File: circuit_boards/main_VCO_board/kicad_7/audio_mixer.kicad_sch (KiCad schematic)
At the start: 24 parts, among them U14 TL072

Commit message: Progress on circuit boards
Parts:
- added D1406 (x5): XLMDK65D, LED_THT:LED_D3.0mm, symbol Device:LED
- added R908, R909, R910, R912: 12k, Resistor_SMD:R_0603_1608Metric, symbol Device:R
- added R911: 5k6, Resistor_SMD:R_0603_1608Metric, symbol Device:R
- SW? (x4): value E-Switch_EG2201 -> E-Switch_EG2201B
- SW? (x5): value E-Switch_EG2301 -> E-Switch_EG2301B
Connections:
- net GND: now also D1406.1 (K), D1406.1 (K), D1406.1 (K), D1406.1 (K), D1406.1 (K)
- net +12V: now reaches SW?.1
- net +12V: now also SW?.1, SW?.1, SW?.1, SW?.2, SW?.2
- net at SW?.3: now also R910.1
- net at SW?.3: now also R912.1
- net at RV10.3, SW?.3: now also R911.1
- net at SW?.2: now also R909.1
- net at SW?.2: now also R908.1
- new net: D1406.2 (A), R908.2
- new net: D1406.2 (A), R909.2
- new net: D1406.2 (A), R910.2
- new net: D1406.2 (A), R911.2
- new net: D1406.2 (A), R912.2
- no-connect marks 14 -> 4
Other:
- note added: "AUDIO SOURCE ENABLED INDICATORS"
- moved on the sheet: C901, R901, R902, R903, R904, R905, R906, R907, RV10, RV11, RV7, RV8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

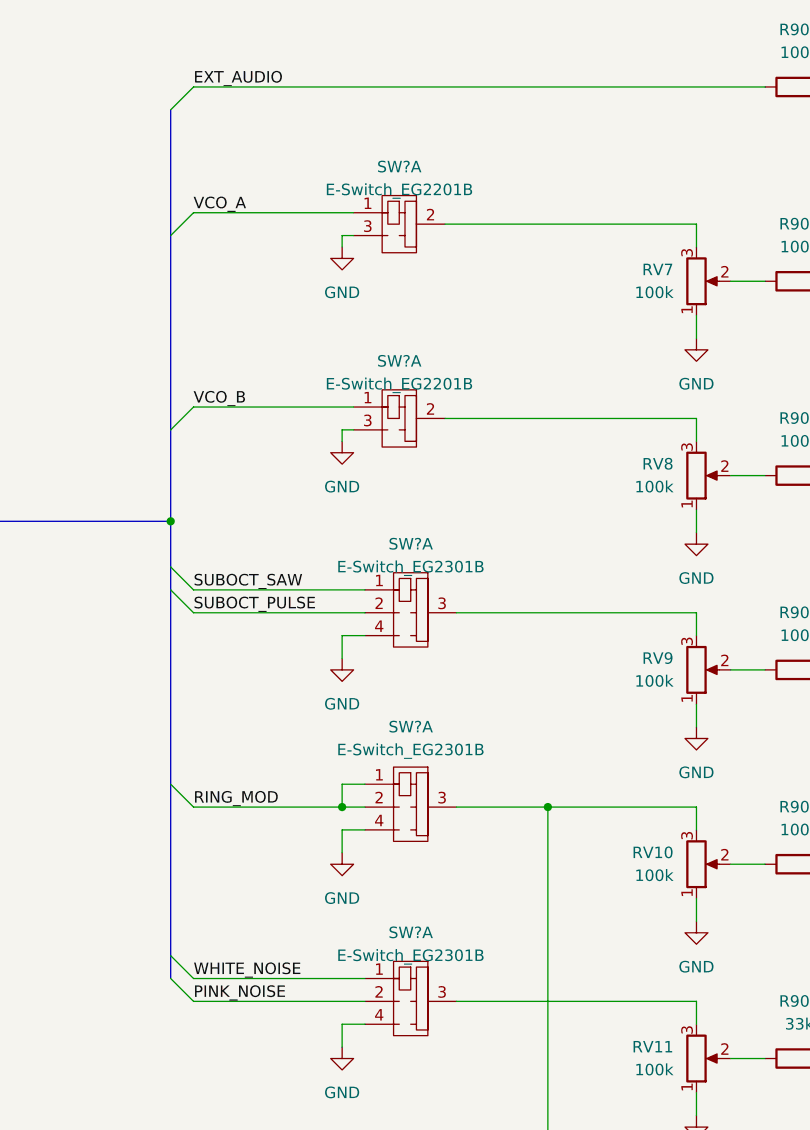
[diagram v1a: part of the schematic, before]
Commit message: Update PCBs, tweak vals, add VCF CV from DAC
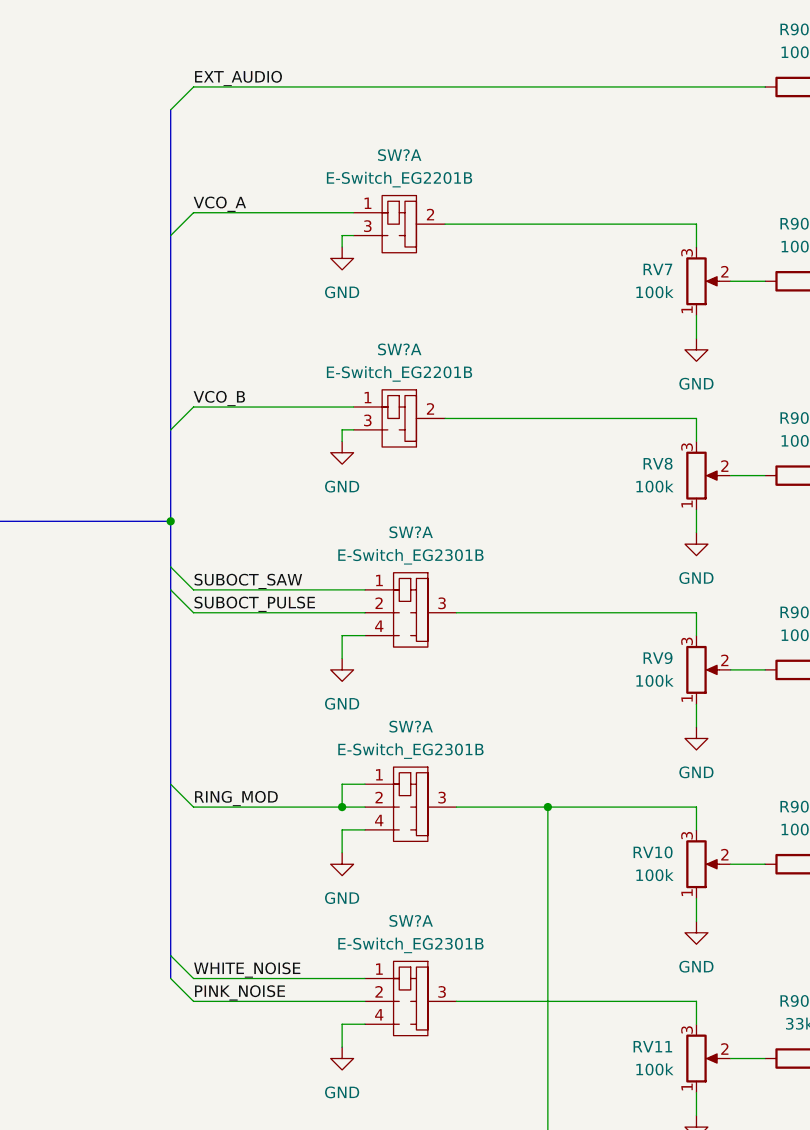
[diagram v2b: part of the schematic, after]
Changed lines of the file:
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@@
   )
   (symbol (lib_id "custom_symbols:E-Switch_EG2201") (at 107.95 63.5 0) (mirror y) (unit 1)
-    (in_bom yes) (on_board yes) (dnp no) (fields_autoplaced)
-    (property "Reference" "SW?" (at 107.95 57.15 0)
-      (effects (font (size 1.27 1.27)))
-    )
-    (property "Value" "E-Switch_EG2201B" (at 107.95 59.69 0)
+    (in_bom yes) (on_board yes) (dnp no)
+    (property "Reference" "SW?" (at 107.95 55.88 0)
+      (effects (font (size 1.27 1.27)))
+    )
+    (property "Value" "E-Switch_EG2201B" (at 107.95 58.42 0)
       (effects (font (size 1.27 1.27)))
     )
@@
   )
   (symbol (lib_id "custom_symbols:E-Switch_EG2201") (at 107.95 41.91 0) (mirror y) (unit 1)
-    (in_bom yes) (on_board yes) (dnp no) (fields_autoplaced)
-    (property "Reference" "SW?" (at 107.95 35.56 0)
-      (effects (font (size 1.27 1.27)))
-    )
-    (property "Value" "E-Switch_EG2201B" (at 107.95 38.1 0)
+    (in_bom yes) (on_board yes) (dnp no)
+    (property "Reference" "SW?" (at 107.95 34.29 0)
+      (effects (font (size 1.27 1.27)))
+    )
+    (property "Value" "E-Switch_EG2201B" (at 107.95 36.83 0)
       (effects (font (size 1.27 1.27)))
     )
@@
   )
   (symbol (lib_id "custom_symbols:E-Switch_EG2301") (at 109.22 85.09 0) (mirror y) (unit 1)
-    (in_bom yes) (on_board yes) (dnp no) (fields_autoplaced)
-    (property "Reference" "SW?" (at 109.22 77.47 0)
-      (effects (font (size 1.27 1.27)))
-    )
-    (property "Value" "E-Switch_EG2301B" (at 109.22 80.01 0)
+    (in_bom yes) (on_board yes) (dnp no)
+    (property "Reference" "SW?" (at 109.22 76.2 0)
+      (effects (font (size 1.27 1.27)))
+    )
+    (property "Value" "E-Switch_EG2301B" (at 109.22 78.74 0)
       (effects (font (size 1.27 1.27)))
     )
@@
   )
   (symbol (lib_id "custom_symbols:E-Switch_EG2301") (at 109.22 128.27 0) (mirror y) (unit 1)
-    (in_bom yes) (on_board yes) (dnp no) (fields_autoplaced)
-    (property "Reference" "SW?" (at 109.22 120.65 0)
-      (effects (font (size 1.27 1.27)))
-    )
-    (property "Value" "E-Switch_EG2301B" (at 109.22 123.19 0)
-      (effects (font (size 1.27 1.27)))
-    )
+    (in_bom yes) (on_board yes) (dnp no)
+    (property "Reference" "SW?" (at 109.22 119.38 0)
+      (effects (font (size 1.27 1.27)))
+    )
+    (property "Value" "E-Switch_EG2301B" (at 109.22 121.92 0)
+      (effects (font (size 1.27 1.27)))
+    )

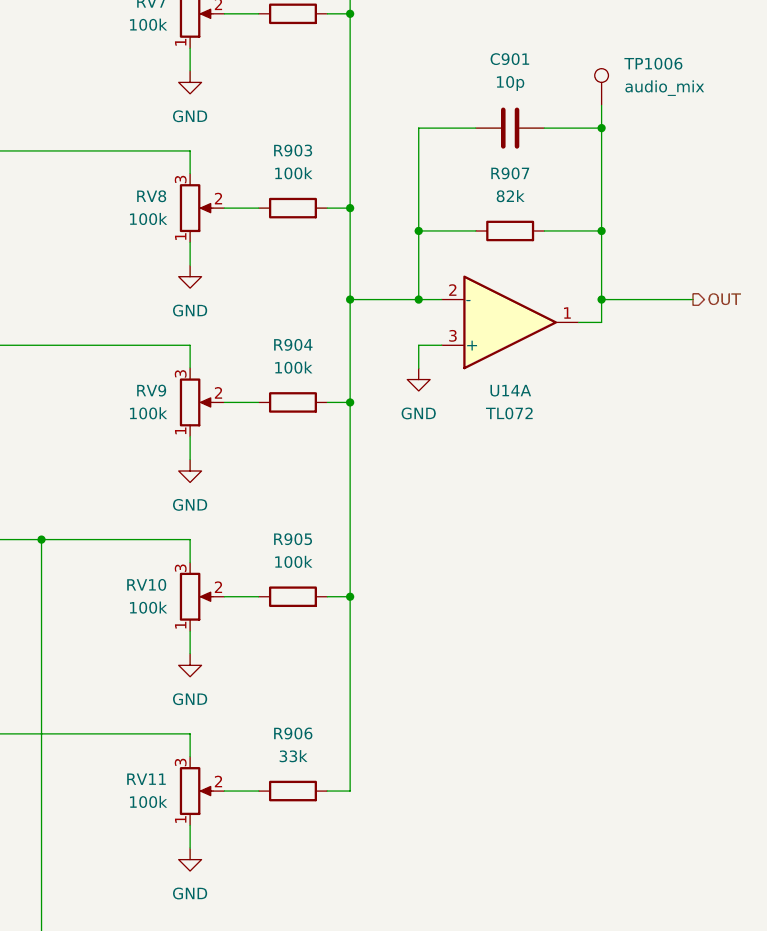
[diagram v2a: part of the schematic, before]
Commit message: Tweaks to VCO R values
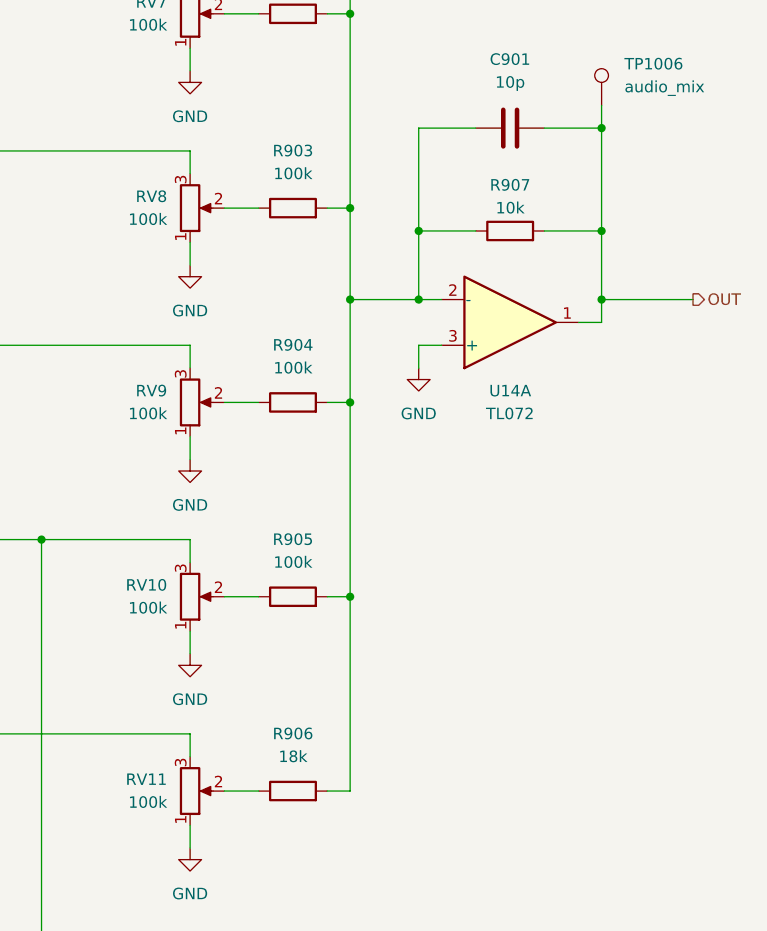
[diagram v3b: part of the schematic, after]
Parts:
- R906: value 33k -> 18k
- R907: value 82k -> 10k
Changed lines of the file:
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@@
   )
   (symbol (lib_id "Device:R") (at 152.4 134.62 90) (unit 1)
-    (in_bom yes) (on_board yes) (dnp no) (fields_autoplaced)
+    (in_bom yes) (on_board yes) (dnp no)
     (property "Reference" "R906" (at 152.4 128.27 90)
       (effects (font (size 1.27 1.27)))
     )
-    (property "Value" "33k" (at 152.4 130.81 90)
+    (property "Value" "18k" (at 152.4 130.81 90)
       (effects (font (size 1.27 1.27)))
     )
@@
   (symbol (lib_id "Device:R") (at 176.53 72.39 90) (unit 1)
     (in_bom yes) (on_board yes) (dnp no) (fields_autoplaced)
-    (property "Reference" "R907" (at 176.53 66.04 90)
-      (effects (font (size 1.27 1.27)))
-    )
-    (property "Value" "82k" (at 176.53 68.58 90)
-      (effects (font (size 1.27 1.27)))
-    )
+    (property "Reference" "R907" (at 176.53 67.31 90)
+      (effects (font (size 1.27 1.27)))
+    )
+    (property "Value" "10k" (at 176.53 69.85 90)
+      (effects (font (size 1.27 1.27)))
+    )

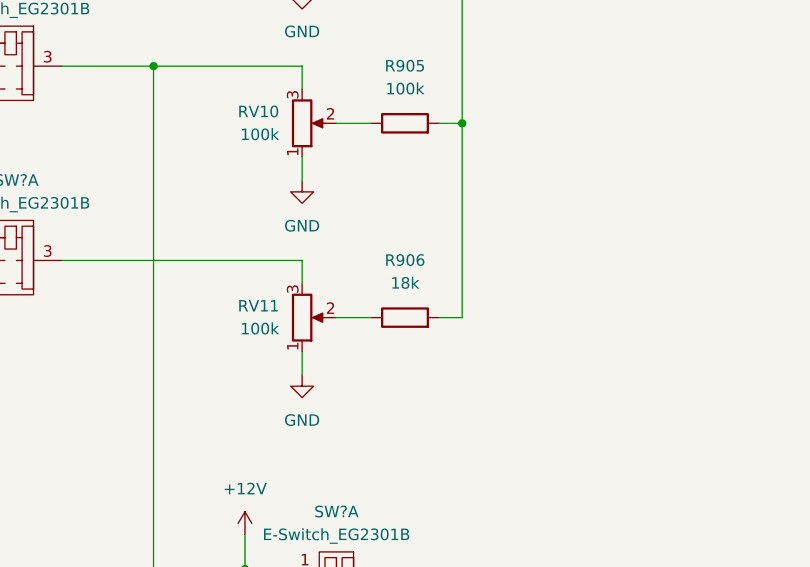
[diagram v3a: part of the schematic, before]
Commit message: Resistor tweaks while evaluating 1st build
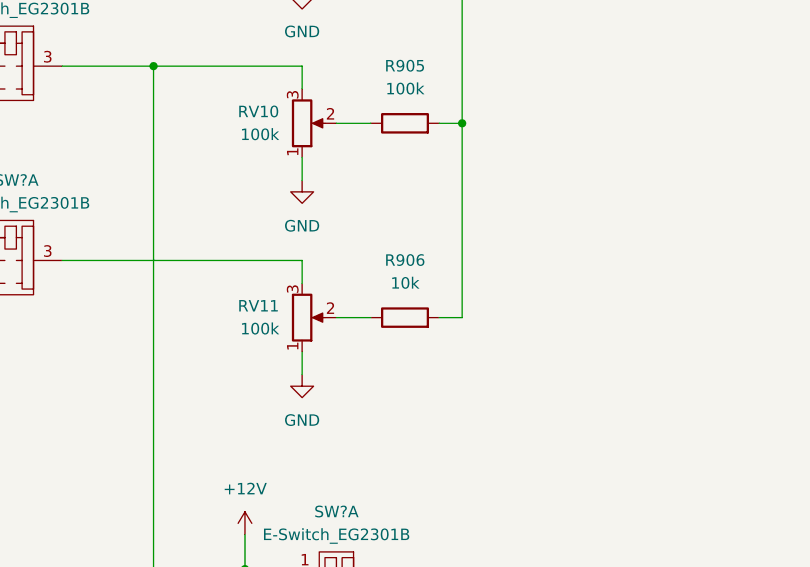
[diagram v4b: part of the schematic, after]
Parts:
- R906: value 18k -> 10k
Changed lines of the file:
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@@
       (effects (font (size 1.27 1.27)))
     )
-    (property "Value" "18k" (at 152.4 130.81 90)
+    (property "Value" "10k" (at 152.4 130.81 90)
       (effects (font (size 1.27 1.27)))
     )

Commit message: Add potentiometer 3d model to VCO and MOD boards
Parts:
- RV10, RV11, RV7, RV8, RV9: footprint Potentiometer_THT:Potentiometer_Alpha_RD901F-40-00D_Single_Vertical -> custom_footprints:Potentiometer_Alpha_RD901F-40-00D_Single_Vertical
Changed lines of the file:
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@@
       (effects (font (size 1.27 1.27)) (justify right))
     )
-    (property "Footprint" "Potentiometer_THT:Potentiometer_Alpha_RD901F-40-00D_Single_Vertical" (at 140.97 91.44 0)
+    (property "Footprint" "custom_footprints:Potentiometer_Alpha_RD901F-40-00D_Single_Vertical" (at 140.97 91.44 0)
       (effects (font (size 1.27 1.27)) hide)
     )
@@
       (effects (font (size 1.27 1.27)) (justify right))
     )
-    (property "Footprint" "Potentiometer_THT:Potentiometer_Alpha_RD901F-40-00D_Single_Vertical" (at 140.97 134.62 0)
+    (property "Footprint" "custom_footprints:Potentiometer_Alpha_RD901F-40-00D_Single_Vertical" (at 140.97 134.62 0)
       (effects (font (size 1.27 1.27)) hide)
     )
@@
       (effects (font (size 1.27 1.27)) (justify right))
     )
-    (property "Footprint" "Potentiometer_THT:Potentiometer_Alpha_RD901F-40-00D_Single_Vertical" (at 140.97 113.03 0)
+    (property "Footprint" "custom_footprints:Potentiometer_Alpha_RD901F-40-00D_Single_Vertical" (at 140.97 113.03 0)
       (effects (font (size 1.27 1.27)) hide)
     )
@@
       (effects (font (size 1.27 1.27)) (justify right))
     )
-    (property "Footprint" "Potentiometer_THT:Potentiometer_Alpha_RD901F-40-00D_Single_Vertical" (at 140.97 69.85 0)
+    (property "Footprint" "custom_footprints:Potentiometer_Alpha_RD901F-40-00D_Single_Vertical" (at 140.97 69.85 0)
       (effects (font (size 1.27 1.27)) hide)
     )
@@
       (effects (font (size 1.27 1.27)) (justify right))
     )
-    (property "Footprint" "Potentiometer_THT:Potentiometer_Alpha_RD901F-40-00D_Single_Vertical" (at 140.97 48.26 0)
-      (effects (font (size 1.27 1.27)) hide)
-    )
+    (property "Footprint" "custom_footprints:Potentiometer_Alpha_RD901F-40-00D_Single_Vertical" (at 140.97 48.26 0)
+      (effects (font (size 1.27 1.27)) hide)
+    )
